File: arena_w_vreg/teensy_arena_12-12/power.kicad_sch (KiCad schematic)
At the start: 50 parts, among them J1 Barrel_Jack, SW1 SW_SPDT, U10 AZ1084-5.0, U11 AZ1084-5.0, U12 AZ1084-5.0, U13 AZ1084-5.0, U14 AZ1084-5.0, U15 AZ1084-5.0, U16 AZ1084-5.0, U17 AZ1084-5.0, U6 AZ1084-5.0, U7 AZ1084-5.0, U8 AZ1084-5.0, U9 AZ1084-5.0

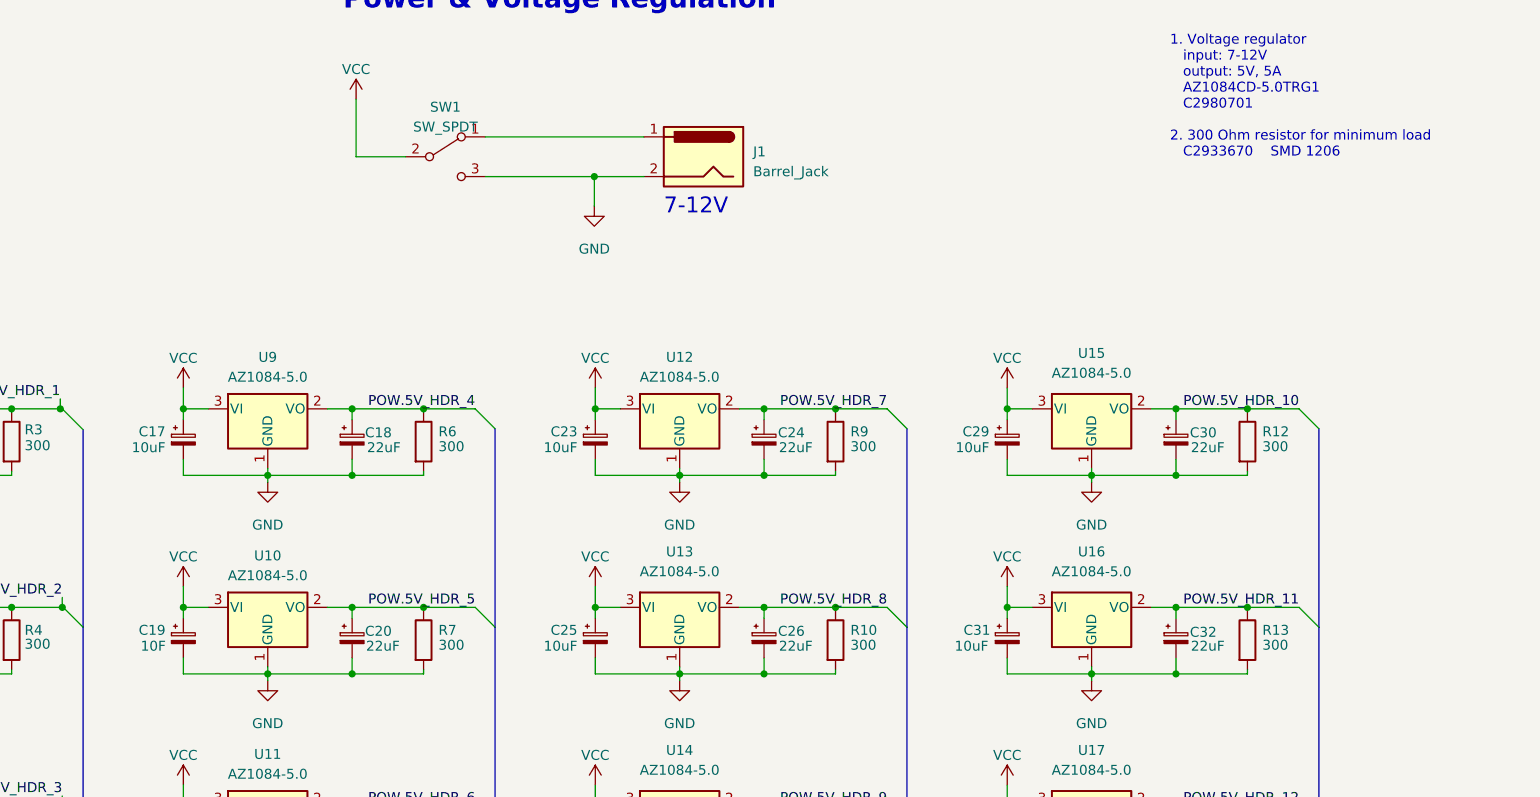
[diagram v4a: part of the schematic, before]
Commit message: Completed initial version of fab files.
Note, there is an issue with the placement of the voltage regulators
which needs to be resolved. Discrepancy between kicad and JLCPCB.
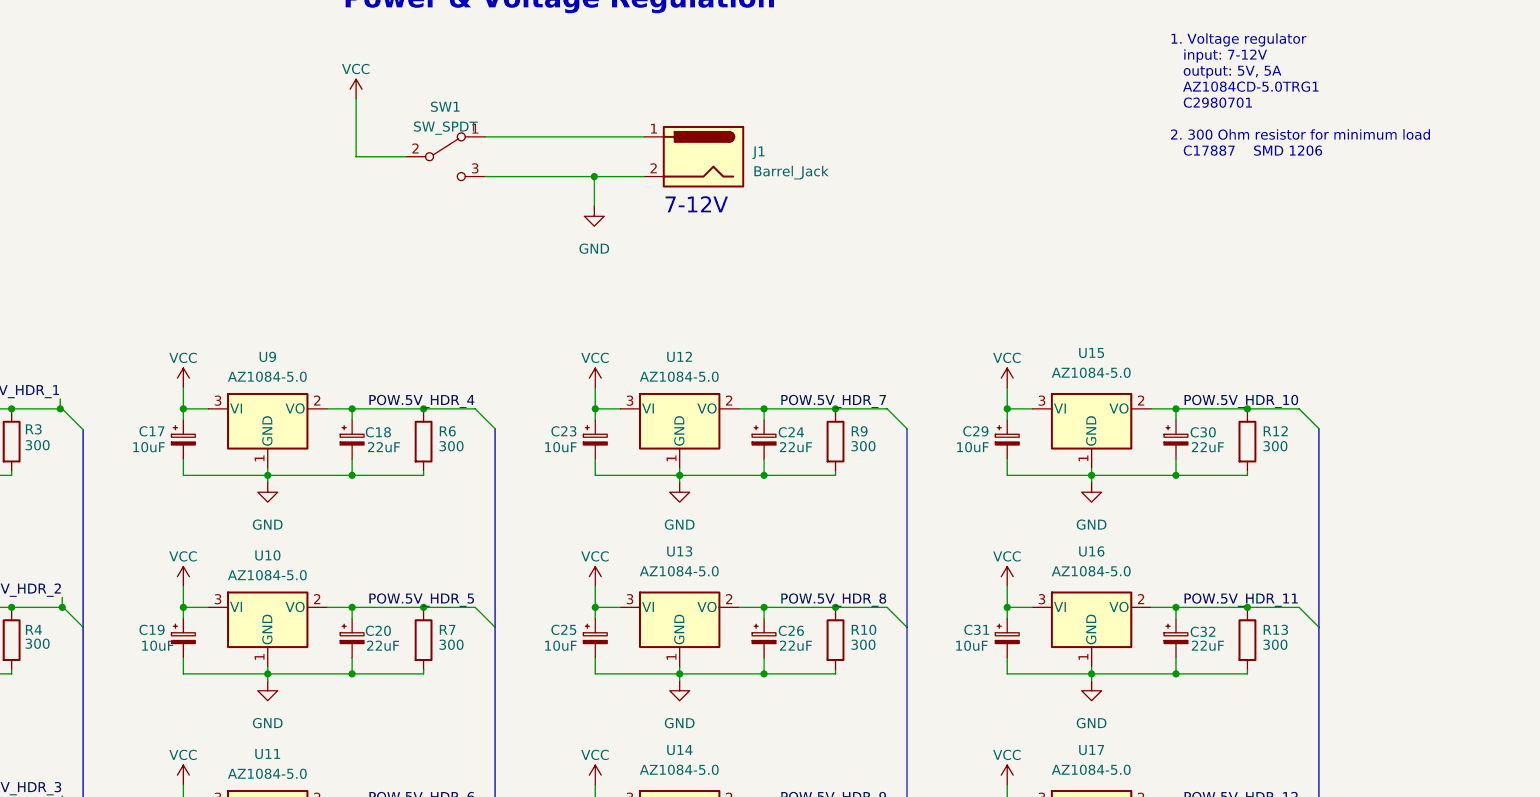
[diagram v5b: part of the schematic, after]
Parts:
- C19: value 10F -> 10uF
- R10, R11, R12, R13, R14, R3, R4, R5, R6, R7, R8, R9: footprint Capacitor_SMD:C_1206_3216Metric -> Resistor_SMD:R_1206_3216Metric
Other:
- note added: "1. Voltage regulator input: 7-12V output: 5V, 5A AZ1084CD-5.0TRG1 C2980701 2. 300 Ohm resistor for minimum load C17887 SMD 1206"
- note removed: "1. Voltage regulator input: 7-12V output: 5V, 5A AZ1084CD-5.0TRG1 C2980701 2. 300 Ohm resistor for minimum load C2933670 SMD 1206"
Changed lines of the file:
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@@
     (effects (font (size 2.032 2.032)) (justify left bottom))
   )
-  (text "1. Voltage regulator\n   input: 7-12V\n   output: 5V, 5A\n   AZ1084CD-5.0TRG1\n   C2980701\n\n2. 300 Ohm resistor for minimum load\n   C2933670    SMD 1206"
+  (text "1. Voltage regulator\n   input: 7-12V\n   output: 5V, 5A\n   AZ1084CD-5.0TRG1\n   C2980701\n\n2. 300 Ohm resistor for minimum load\n   C17887    SMD 1206"
     (at 220.98 39.878 0)
     (effects (font (size 1.27 1.27)) (justify left bottom))
@@
       (effects (font (size 1.27 1.27)) (justify left))
     )
-    (property "Footprint" "Capacitor_SMD:C_1206_3216Metric" (at 70.993 126.873 90)
+    (property "Footprint" "Resistor_SMD:R_1206_3216Metric" (at 70.993 126.873 90)
       (effects (font (size 1.27 1.27)) hide)
     )
@@
       (effects (font (size 1.27 1.27)) (justify left))
     )
-    (property "Footprint" "Capacitor_SMD:C_1206_3216Metric" (at 176.403 126.873 90)
+    (property "Footprint" "Resistor_SMD:R_1206_3216Metric" (at 176.403 126.873 90)
       (effects (font (size 1.27 1.27)) hide)
     )
@@
       (effects (font (size 1.27 1.27)) (justify left))
     )
-    (property "Footprint" "Capacitor_SMD:C_1206_3216Metric" (at 229.108 76.073 90)
+    (property "Footprint" "Resistor_SMD:R_1206_3216Metric" (at 229.108 76.073 90)
       (effects (font (size 1.27 1.27)) hide)
     )
@@
       (effects (font (size 1.27 1.27)) (justify left))
     )
-    (property "Footprint" "Capacitor_SMD:C_1206_3216Metric" (at 229.108 101.473 90)
+    (property "Footprint" "Resistor_SMD:R_1206_3216Metric" (at 229.108 101.473 90)
       (effects (font (size 1.27 1.27)) hide)
     )
@@
       (effects (font (size 1.27 1.27)) (justify left))
     )
-    (property "Footprint" "Capacitor_SMD:C_1206_3216Metric" (at 70.993 101.473 90)
+    (property "Footprint" "Resistor_SMD:R_1206_3216Metric" (at 70.993 101.473 90)
       (effects (font (size 1.27 1.27)) hide)
     )
@@
       (effects (font (size 1.27 1.27)) (justify left))
     )
-    (property "Footprint" "Capacitor_SMD:C_1206_3216Metric" (at 229.108 126.873 90)
+    (property "Footprint" "Resistor_SMD:R_1206_3216Metric" (at 229.108 126.873 90)
       (effects (font (size 1.27 1.27)) hide)
     )
@@
       (effects (font (size 1.27 1.27)) (justify left))
     )
-    (property "Footprint" "Capacitor_SMD:C_1206_3216Metric" (at 123.698 76.073 90)
+    (property "Footprint" "Resistor_SMD:R_1206_3216Metric" (at 123.698 76.073 90)
       (effects (font (size 1.27 1.27)) hide)
     )
@@
       (effects (font (size 1.27 1.27)) (justify left))
     )
-    (property "Value" "10F" (at 89.281 102.235 0)
+    (property "Value" "10uF" (at 89.281 102.235 0)
       (effects (font (size 1.27 1.27)) (justify left))
     )
@@
       (effects (font (size 1.27 1.27)) (justify left))
     )
-    (property "Footprint" "Capacitor_SMD:C_1206_3216Metric" (at 176.403 101.473 90)
+    (property "Footprint" "Resistor_SMD:R_1206_3216Metric" (at 176.403 101.473 90)
       (effects (font (size 1.27 1.27)) hide)
     )
@@
       (effects (font (size 1.27 1.27)) (justify left))
     )
-    (property "Footprint" "Capacitor_SMD:C_1206_3216Metric" (at 123.698 126.873 90)
+    (property "Footprint" "Resistor_SMD:R_1206_3216Metric" (at 123.698 126.873 90)
       (effects (font (size 1.27 1.27)) hide)
     )
@@
       (effects (font (size 1.27 1.27)) (justify left))
     )
-    (property "Footprint" "Capacitor_SMD:C_1206_3216Metric" (at 123.698 101.473 90)
+    (property "Footprint" "Resistor_SMD:R_1206_3216Metric" (at 123.698 101.473 90)
       (effects (font (size 1.27 1.27)) hide)
     )
@@
       (effects (font (size 1.27 1.27)) (justify left))
     )
-    (property "Footprint" "Capacitor_SMD:C_1206_3216Metric" (at 70.993 76.073 90)
+    (property "Footprint" "Resistor_SMD:R_1206_3216Metric" (at 70.993 76.073 90)
       (effects (font (size 1.27 1.27)) hide)
     )
@@
       (effects (font (size 1.27 1.27)) (justify left))
     )
-    (property "Footprint" "Capacitor_SMD:C_1206_3216Metric" (at 176.403 76.073 90)
-      (effects (font (size 1.27 1.27)) hide)
-    )
+    (property "Footprint" "Resistor_SMD:R_1206_3216Metric" (at 176.403 76.073 90)
+      (effects (font (size 1.27 1.27)) hide)
+    )

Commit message: Fixed issue with AZ1084CD-5.0TRG1.
Note, need to do re-route the voltage regulators and redo the CPL file and gerber files.
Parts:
- U10, U11, U12, U13, U14, U15, U16, U17, U6, U7, U8, U9: footprint Package_TO_SOT_SMD:TO-252-3_TabPin2 -> arena_custom:TO-252
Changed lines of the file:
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@@
       (effects (font (size 1.27 1.27)))
     )
-    (property "Footprint" "Package_TO_SOT_SMD:TO-252-3_TabPin2" (at 158.242 116.332 0)
+    (property "Footprint" "arena_custom:TO-252" (at 158.242 116.332 0)
       (effects (font (size 1.27 1.27) italic) hide)
     )
@@
       (effects (font (size 1.27 1.27)))
     )
-    (property "Footprint" "Package_TO_SOT_SMD:TO-252-3_TabPin2" (at 210.947 90.932 0)
+    (property "Footprint" "arena_custom:TO-252" (at 210.947 90.932 0)
       (effects (font (size 1.27 1.27) italic) hide)
     )
@@
       (effects (font (size 1.27 1.27)))
     )
-    (property "Footprint" "Package_TO_SOT_SMD:TO-252-3_TabPin2" (at 210.947 116.332 0)
+    (property "Footprint" "arena_custom:TO-252" (at 210.947 116.332 0)
       (effects (font (size 1.27 1.27) italic) hide)
     )
@@
       (effects (font (size 1.27 1.27)))
     )
-    (property "Footprint" "Package_TO_SOT_SMD:TO-252-3_TabPin2" (at 105.537 90.932 0)
+    (property "Footprint" "arena_custom:TO-252" (at 105.537 90.932 0)
       (effects (font (size 1.27 1.27) italic) hide)
     )
@@
       (effects (font (size 1.27 1.27)))
     )
-    (property "Footprint" "Package_TO_SOT_SMD:TO-252-3_TabPin2" (at 105.537 116.332 0)
+    (property "Footprint" "arena_custom:TO-252" (at 105.537 116.332 0)
       (effects (font (size 1.27 1.27) italic) hide)
     )
@@
       (effects (font (size 1.27 1.27)))
     )
-    (property "Footprint" "Package_TO_SOT_SMD:TO-252-3_TabPin2" (at 105.537 65.532 0)
+    (property "Footprint" "arena_custom:TO-252" (at 105.537 65.532 0)
       (effects (font (size 1.27 1.27) italic) hide)
     )
@@
       (effects (font (size 1.27 1.27)))
     )
-    (property "Footprint" "Package_TO_SOT_SMD:TO-252-3_TabPin2" (at 158.242 90.932 0)
+    (property "Footprint" "arena_custom:TO-252" (at 158.242 90.932 0)
       (effects (font (size 1.27 1.27) italic) hide)
     )
@@
       (effects (font (size 1.27 1.27)))
     )
-    (property "Footprint" "Package_TO_SOT_SMD:TO-252-3_TabPin2" (at 52.832 90.932 0)
+    (property "Footprint" "arena_custom:TO-252" (at 52.832 90.932 0)
       (effects (font (size 1.27 1.27) italic) hide)
     )
@@
       (effects (font (size 1.27 1.27)))
     )
-    (property "Footprint" "Package_TO_SOT_SMD:TO-252-3_TabPin2" (at 52.832 65.532 0)
+    (property "Footprint" "arena_custom:TO-252" (at 52.832 65.532 0)
       (effects (font (size 1.27 1.27) italic) hide)
     )
@@
       (effects (font (size 1.27 1.27)))
     )
-    (property "Footprint" "Package_TO_SOT_SMD:TO-252-3_TabPin2" (at 158.242 65.532 0)
+    (property "Footprint" "arena_custom:TO-252" (at 158.242 65.532 0)
       (effects (font (size 1.27 1.27) italic) hide)
     )
@@
       (effects (font (size 1.27 1.27)))
     )
-    (property "Footprint" "Package_TO_SOT_SMD:TO-252-3_TabPin2" (at 210.947 65.532 0)
+    (property "Footprint" "arena_custom:TO-252" (at 210.947 65.532 0)
       (effects (font (size 1.27 1.27) italic) hide)
     )
@@
       (effects (font (size 1.27 1.27)))
     )
-    (property "Footprint" "Package_TO_SOT_SMD:TO-252-3_TabPin2" (at 52.832 116.332 0)
+    (property "Footprint" "arena_custom:TO-252" (at 52.832 116.332 0)
       (effects (font (size 1.27 1.27) italic) hide)
     )

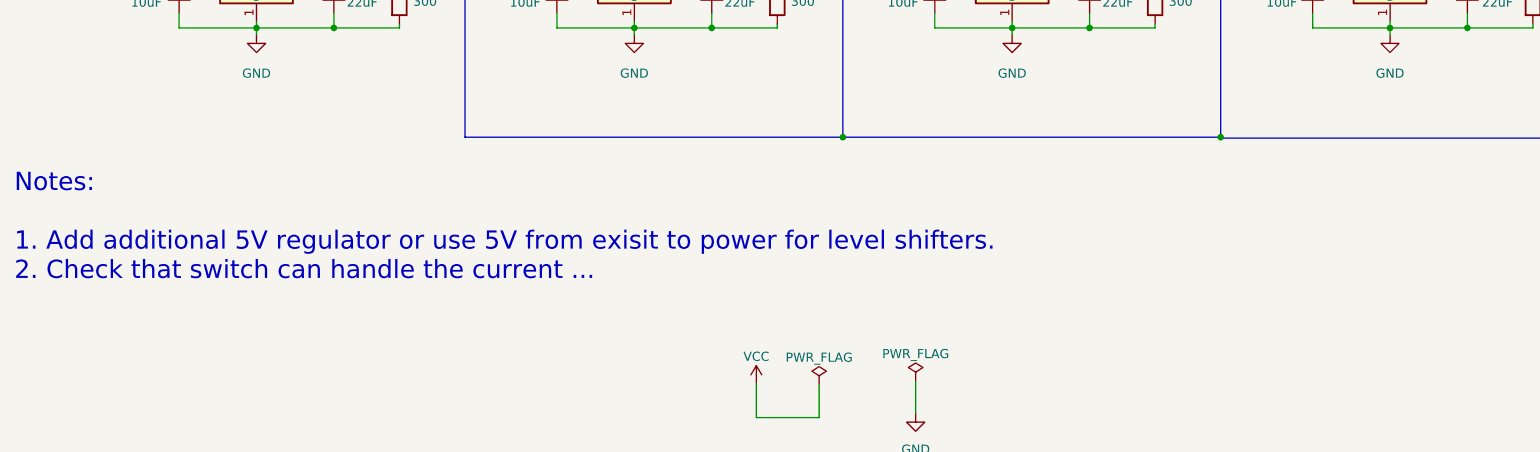
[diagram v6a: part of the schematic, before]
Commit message: Removed old notes from schematic pdf.
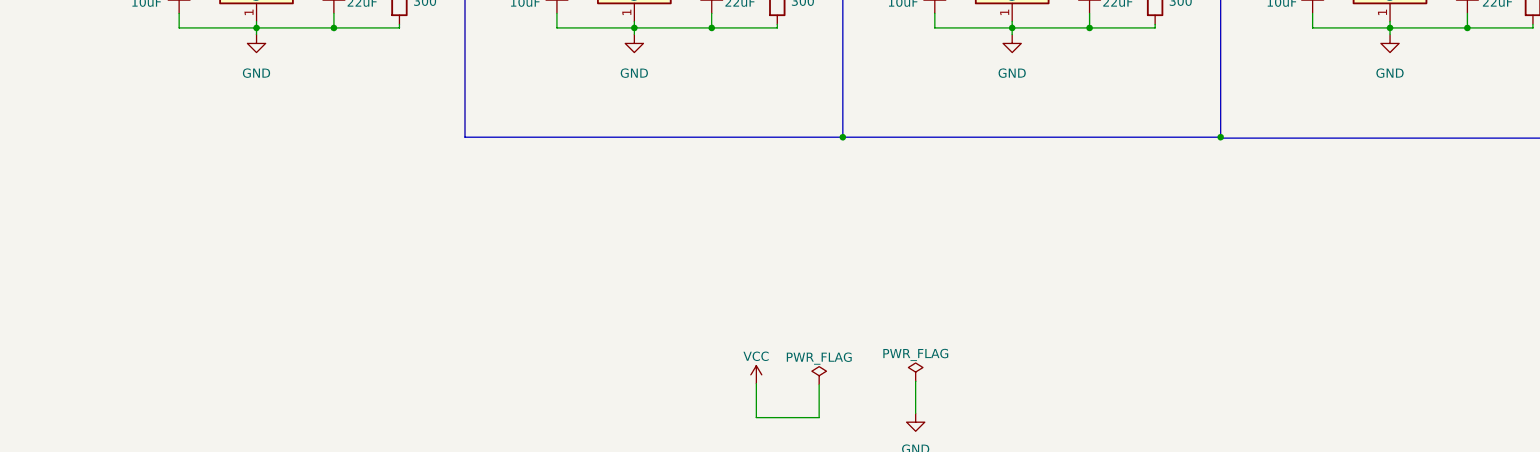
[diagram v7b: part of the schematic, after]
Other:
- note removed: "Notes: 1. Add additional 5V regulator or use 5V from exisit to power for level shifters. 2. Check that switch can handle the current ..."
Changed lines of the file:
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@@
     (stroke (width 0) (type default))
-  )
-  (text "Notes:\n\n1. Add additional 5V regulator or use 5V from exisit to power for level shifters. \n2. Check that switch can handle the current ..."
-    (at 19.05 166.624 0)
-    (effects (font (size 2.54 2.54)) (justify left bottom))
   )
   (text "7-12V" (at 156.21 47.244 0)
